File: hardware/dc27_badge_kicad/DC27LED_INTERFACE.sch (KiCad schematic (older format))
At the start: 13 parts, among them U301 IS31FL3216A

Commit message: add gerbers for prototype
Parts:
- removed C307: 1uF, Capacitor_SMD:C_0603_1608Metric, symbol Device:C
- removed C308: 0.1uF, Capacitor_SMD:C_0603_1608Metric, symbol Device:C
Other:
- note added: "note - on pcb avcc and dvcc very close, removing bypass caps here."
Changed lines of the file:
@@
 AVCC
 Wire Wire Line
-	2700 3250 3100 3250
+	2700 3250 3000 3250
 Connection ~ 2700 3250
-$Comp
-L Device:C C307
-U 1 1 5BDAFD76
-P 2100 4450
-F 0 "C307" H 2215 4496 50  0000 L CNN
-F 1 "1uF" H 2215 4405 50  0000 L CNN
-F 2 "Capacitor_SMD:C_0603_1608Metric" H 2138 4300 50  0001 C CNN
-F 3 "~" H 2100 4450 50  0001 C CNN
-	1    2100 4450
-	1    0    0    -1
-$EndComp
-$Comp
-L Device:C C308
-U 1 1 5BDAFD7C
-P 2700 4450
-F 0 "C308" H 2815 4496 50  0000 L CNN
-F 1 "0.1uF" H 2815 4405 50  0000 L CNN
-F 2 "Capacitor_SMD:C_0603_1608Metric" H 2738 4300 50  0001 C CNN
-F 3 "~" H 2700 4450 50  0001 C CNN
-	1    2700 4450
-	1    0    0    -1
-$EndComp
-Wire Wire Line
-	2100 4250 2100 4300
-Wire Wire Line
-	2100 4250 2700 4250
-Wire Wire Line
-	2700 4250 2700 4300
-Connection ~ 2100 4250
-$Comp
-L power:GND #PWR0311
-U 1 1 5BDAFD87
-P 2100 4800
-F 0 "#PWR0311" H 2100 4550 50  0001 C CNN
-F 1 "GND" H 2105 4627 50  0000 C CNN
-F 2 "" H 2100 4800 50  0001 C CNN
-F 3 "" H 2100 4800 50  0001 C CNN
-	1    2100 4800
-	1    0    0    -1
-$EndComp
-$Comp
-L power:GND #PWR0312
-U 1 1 5BDAFD8D
-P 2700 4800
-F 0 "#PWR0312" H 2700 4550 50  0001 C CNN
-F 1 "GND" H 2705 4627 50  0000 C CNN
-F 2 "" H 2700 4800 50  0001 C CNN
-F 3 "" H 2700 4800 50  0001 C CNN
-	1    2700 4800
-	1    0    0    -1
-$EndComp
-Wire Wire Line
-	2100 4600 2100 4800
-Wire Wire Line
-	2700 4600 2700 4800
 Text GLabel 3100 4250 2    50   Output ~ 0
 DVCC
-Wire Wire Line
-	2700 4250 3100 4250
-Connection ~ 2700 4250
 Text GLabel 5450 1850 1    50   Input ~ 0
 PVCC1
@@
 	1700 5200 2100 5200
 Wire Wire Line
-	1700 4250 2100 4250
-Connection ~ 1700 4250
-Wire Wire Line
-	1700 4250 1700 5200
-Wire Wire Line
 	1700 3250 2100 3250
 Connection ~ 1700 3250
-Wire Wire Line
-	1700 3250 1700 4250
 Wire Wire Line
 	1700 2250 2100 2250
@@
 	1    0    0    -1
 $EndComp
+Wire Wire Line
+	1700 3250 1700 5200
+Wire Wire Line
+	3000 3250 3000 4250
+Wire Wire Line
+	3000 4250 3100 4250
+Connection ~ 3000 3250
+Wire Wire Line
+	3000 3250 3100 3250
+Text Notes 1850 4500 0    50   ~ 0
+note - on pcb avcc and dvcc very close, removing bypass caps here.
 $EndSCHEMATC

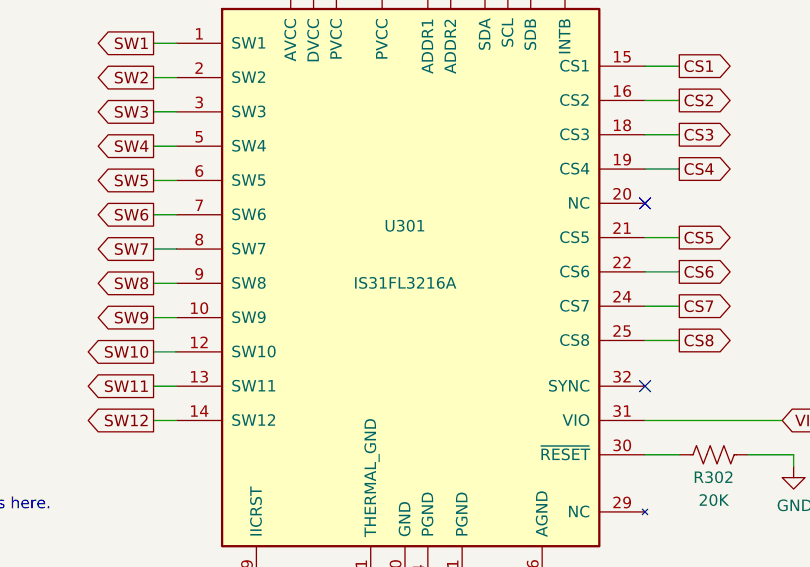
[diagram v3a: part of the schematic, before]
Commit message: update schematic and re-check in gerbers
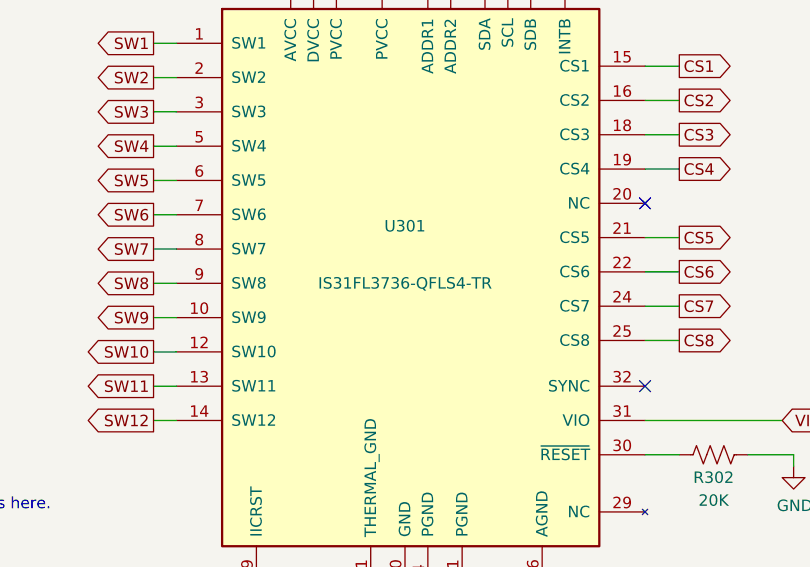
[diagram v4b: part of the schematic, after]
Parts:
- U301: value IS31FL3216A -> IS31FL3736-QFLS4-TR
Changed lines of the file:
@@
 P 5750 3450
 F 0 "U301" H 5750 3650 50  0000 C CNN
-F 1 "IS31FL3216A" H 5750 3400 50  0000 C CNN
+F 1 "IS31FL3736-QFLS4-TR" H 5750 3400 50  0000 C CNN
 F 2 "Package_DFN_QFN:QFN-40-1EP_5x5mm_P0.4mm_EP3.6x3.6mm" H 5700 1600 50  0001 C CNN
 F 3 "" H 4120 4590 50  0001 C CNN

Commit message: update gerbers for R302 issue
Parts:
- R302: footprint Resistor_SMD:R_0603_1608Metric -> Resistor_SMD:R_0805_2012Metric
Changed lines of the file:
@@
 F 0 "R302" V 7200 4250 50  0000 C CNN
 F 1 "20K" V 7300 4250 50  0000 C CNN
-F 2 "Resistor_SMD:R_0603_1608Metric" V 7140 4240 50  0001 C CNN
+F 2 "Resistor_SMD:R_0805_2012Metric" V 7140 4240 50  0001 C CNN
 F 3 "~" H 7100 4250 50  0001 C CNN
 	1    7100 4250
